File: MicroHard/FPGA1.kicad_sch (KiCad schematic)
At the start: 1 part, among them U4 XC7A100T-FTG256

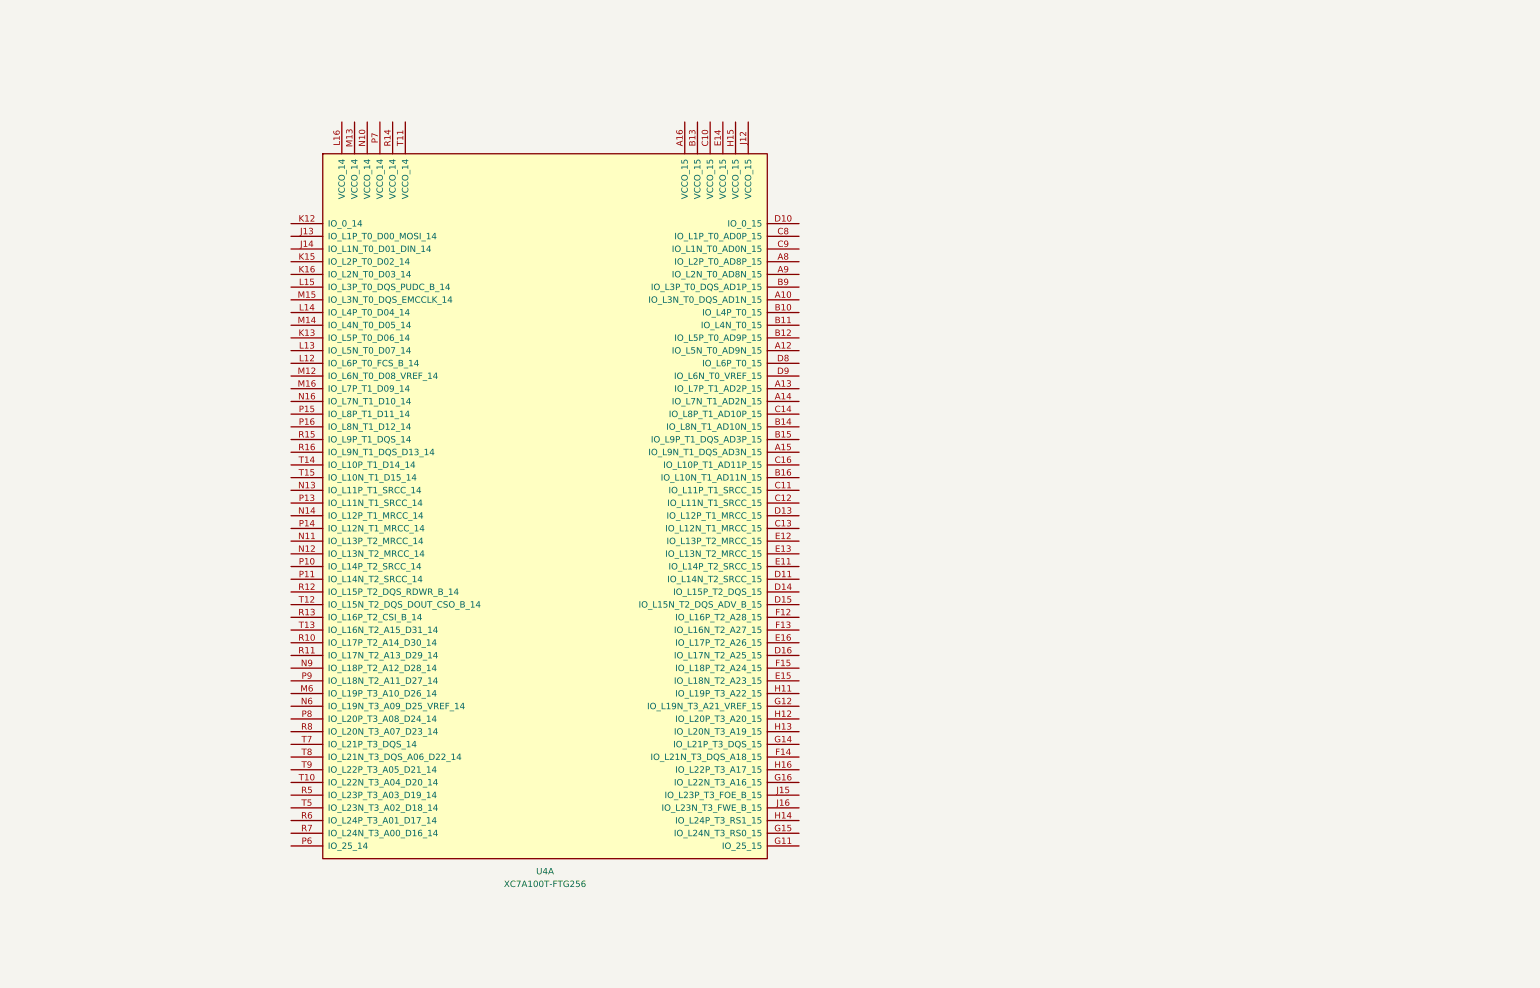
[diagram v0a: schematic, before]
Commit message: feat: finished FPGA config
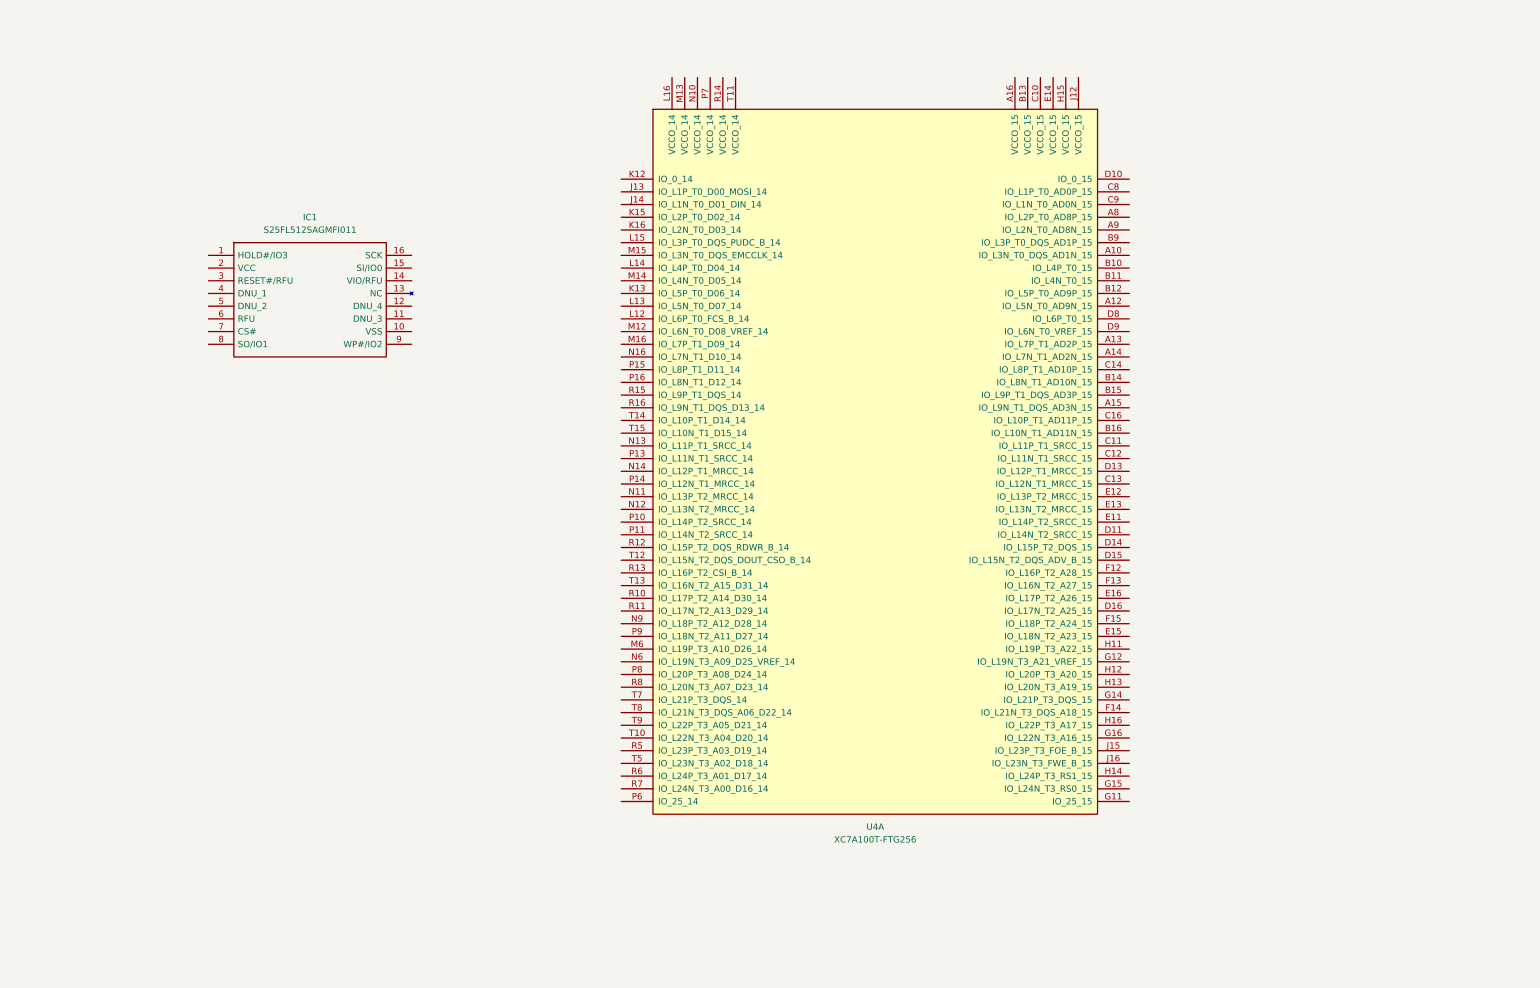
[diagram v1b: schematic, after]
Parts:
- added IC1: S25FL512SAGMFI011, SOIC127P1030X265-16N, symbol S25FL512SAGMFI011:S25FL512SAGMFI011
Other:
- moved on the sheet: U4A
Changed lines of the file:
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@@
 	(paper "A4")
 	(symbol
+		(lib_id "S25FL512SAGMFI011:S25FL512SAGMFI011")
+		(at 24.13 52.07 0)
+		(unit 1)
+		(exclude_from_sim no)
+		(in_bom yes)
+		(on_board yes)
+		(dnp no)
+		(fields_autoplaced yes)
+		(property "Reference" "IC1"
+			(at 44.45 44.45 0)
+			(effects
+				(font
+					(size 1.27 1.27)
+				)
+			)
+		)
+		(property "Value" "S25FL512SAGMFI011"
+			(at 44.45 46.99 0)
+			(effects
+				(font
+					(size 1.27 1.27)
+				)
+			)
+		)
+		(property "Footprint" "SOIC127P1030X265-16N"
+			(at 60.96 49.53 0)
+			(effects
+				(font
+					(size 1.27 1.27)
+				)
+				(justify left)
+				(hide yes)
+			)
+		)
+		(property "Datasheet" "http://www.cypress.com/file/177971/download"
+			(at 60.96 52.07 0)
+			(effects
+				(font
+					(size 1.27 1.27)
+				)
+				(justify left)
+				(hide yes)
+			)
+		)
+		(property "Description" "Flash,512Mbit,QSPI,133MHz,3V,SOIC16 S25FL512SAGMFI011, SPI NOR Flash Memory, 128M x 4 bit, 256M x 2 bit, 512M x 1 bit 512Mbit, 2.7  3.6 V, 16-Pin"
+			(at 24.13 52.07 0)
+			(effects
+				(font
+					(size 1.27 1.27)
+				)
+				(hide yes)
+			)
+		)
+		(property "Description_1" "Flash,512Mbit,QSPI,133MHz,3V,SOIC16 S25FL512SAGMFI011, SPI NOR Flash Memory, 128M x 4 bit, 256M x 2 bit, 512M x 1 bit 512Mbit, 2.7  3.6 V, 16-Pin"
+			(at 60.96 54.61 0)
+			(effects
+				(font
+					(size 1.27 1.27)
+				)
+				(justify left)
+				(hide yes)
+			)
+		)
+		(property "Height" "2.65"
+			(at 60.96 57.15 0)
+			(effects
+				(font
+					(size 1.27 1.27)
+				)
+				(justify left)
+				(hide yes)
+			)
+		)
+		(property "Mouser Part Number" "797-25FL512SAGMFI011"
+			(at 60.96 59.69 0)
+			(effects
+				(font
+					(size 1.27 1.27)
+				)
+				(justify left)
+				(hide yes)
+			)
+		)
+		(property "Mouser Price/Stock" "https://www.mouser.co.uk/ProductDetail/Cypress-Spansion/S25FL512SAGMFI011?qs=rDGpJoRV1kJ%252BPU3pl%252BHK1A%3D%3D"
+			(at 60.96 62.23 0)
+			(effects
+				(font
+					(size 1.27 1.27)
+				)
+				(justify left)
+				(hide yes)
+			)
+		)
+		(property "Manufacturer_Name" "Infineon"
+			(at 60.96 64.77 0)
+			(effects
+				(font
+					(size 1.27 1.27)
+				)
+				(justify left)
+				(hide yes)
+			)
+		)
+		(property "Manufacturer_Part_Number" "S25FL512SAGMFI011"
+			(at 60.96 67.31 0)
+			(effects
+				(font
+					(size 1.27 1.27)
+				)
+				(justify left)
+				(hide yes)
+			)
+		)
+		(pin "7"
+		)
+		(pin "6"
+		)
+		(pin "8"
+		)
+		(pin "1"
+		)
+		(pin "12"
+		)
+		(pin "10"
+		)
+		(pin "11"
+		)
+		(pin "4"
+		)
+		(pin "5"
+		)
+		(pin "13"
+		)
+		(pin "15"
+		)
+		(pin "3"
+		)
+		(pin "9"
+		)
+		(pin "2"
+		)
+		(pin "16"
+		)
+		(pin "14"
+		)
+		(instances
+			(project "MicroHard"
+				(path "/578bd531-a491-4b15-a479-460d159ffc14/e381883e-e672-4900-88a5-08b94f970a88/1131f32d-45e2-48d4-a5b0-b9e8f8db47f2"
+					(reference "IC1")
+					(unit 1)
+				)
+			)
+		)
+	)
+	(symbol
 		(lib_id "FPGA_Xilinx_Artix7:XC7A100T-FTG256")
-		(at 91.44 99.06 0)
+		(at 157.48 90.17 0)
 		(unit 1)
 		(exclude_from_sim no)
@@
 		(fields_autoplaced yes)
 		(property "Reference" "U4"
-			(at 91.44 175.26 0)
+			(at 157.48 166.37 0)
 			(effects
 				(font
@@
 		)
 		(property "Value" "XC7A100T-FTG256"
-			(at 91.44 177.8 0)
+			(at 157.48 168.91 0)
 			(effects
 				(font
@@
 		)
 		(property "Footprint" ""
-			(at 91.44 99.06 0)
+			(at 157.48 90.17 0)
 			(effects
 				(font
@@
 		)
 		(property "Datasheet" ""
-			(at 91.44 99.06 0)
+			(at 157.48 90.17 0)
 			(effects
 				(font
@@
 		)
 		(property "Description" "Artix 7 T 100 XC7A100T-FTG256"
-			(at 91.44 99.06 0)
-			(effects
-				(font
+			(at 157.48 90.17 0)
+			(effects
+				(font

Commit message: feat: finished Flash mem and FPGA Config
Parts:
- removed IC1: S25FL512SAGMFI011, SOIC127P1030X265-16N, symbol S25FL512SAGMFI011:S25FL512SAGMFI011
- added C45: 100u, symbol Device:C_Polarized_US
- added C46, C47: 4.7u, symbol Device:C
- added C48, C49, C50, C51: 470n, symbol Device:C
- added C52: 100n, symbol Device:C
- added R20, R22: 4.7k, symbol Device:R
- added R21: 2.4k, symbol Device:R
- added U5: MT25QL256ABA8ESF-0SIT, symbol MicroHardLibrary:MT25QL256ABA8ESF-0SIT
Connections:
- net DQ0: now reaches U4.J13 (IO_L1P_T0_D00_MOSI_14)
- net DQ0: now also U5.15 (DQ0)
- net DQ1: now reaches U4.J14 (IO_L1N_T0_D01_DIN_14)
- net DQ1: now also U5.8 (DQ1)
- net W#: now reaches U4.K15 (IO_L2P_T0_D02_14)
- net W#: now also R22.2, U5.9 (W#/DQ2)
- net HOLD#: now reaches U4.K16 (IO_L2N_T0_D03_14)
- net HOLD#: now also R20.2, U5.1 (DQ3/HOLD#)
- net CS#: now reaches U4.L12 (IO_L6P_T0_FCS_B_14)
- net CS#: now also R21.2, U5.7 (S#)
- net GND: now reaches U4.L15 (IO_L3P_T0_DQS_PUDC_B_14)
- net GND: now also C45.2, C46.2, C47.2, C48.2, C49.2, C50.2, C51.2, C52.2, U5.10 (Vss)
- net +3.3V: now reaches U4.L16 (VCCO_14)
- net +3.3V: now also U4.M13 (VCCO_14), U4.N10 (VCCO_14), U4.P7 (VCCO_14), U4.R14 (VCCO_14), U4.T11 (VCCO_14), C45.1, C46.1, C47.1, C48.1, C49.1, C50.1, C51.1, C52.1, R20.1, R21.1, R22.1, U5.2 (Vcc)
- new net FPGA_CONFIG_CLOCK: U5.16 (C)
- no-connect marks 0 -> 2
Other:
- moved on the sheet: U4A

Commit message: feat: finished config
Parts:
- added C53: 10n, symbol Device:C
- added C54: 30p, symbol Device:C
- added Y1: CB3-3C-20M000000, CB3-3C-20M000000:OSC_CB3-3C-20M000000, symbol CB3-3C-20M000000:CB3-3C-20M000000
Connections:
- net +3.3V: now also C53.1, Y1.1 (EOH), Y1.4 (VCC)
- net GND: now also C53.2, C54.2, Y1.2 (GND)
- net at U4.N11 (IO_L13P_T2_MRCC_14): now also C54.1, Y1.3 (OUTPUT)
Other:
- note added: "Oscillator with stability +- 50 ppm"

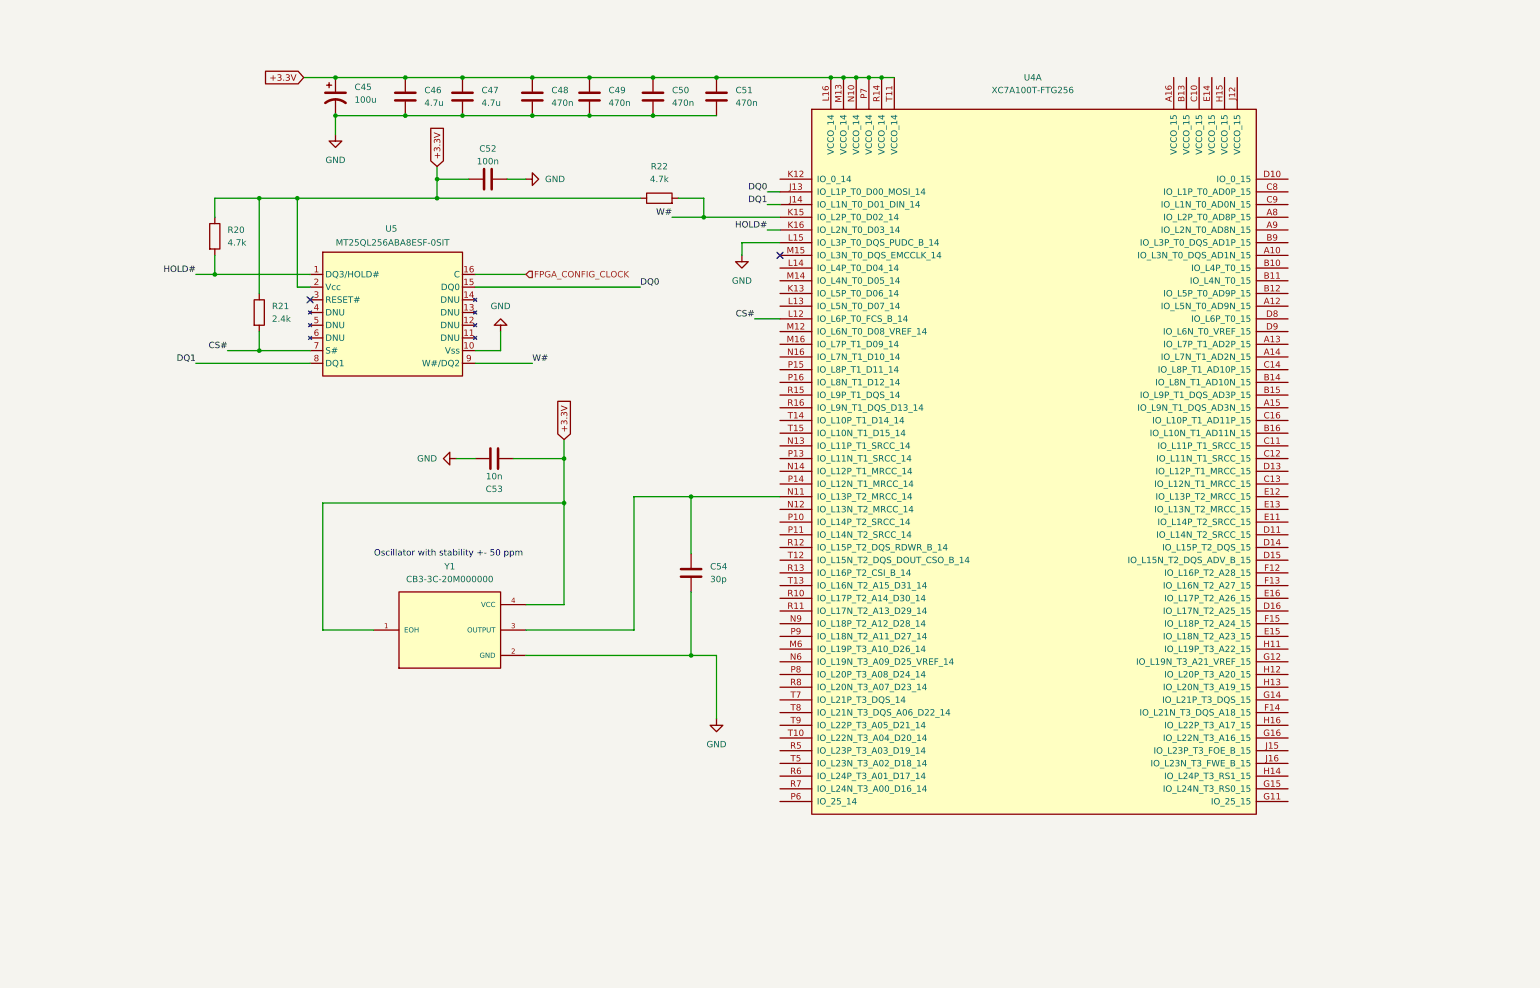
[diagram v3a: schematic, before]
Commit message: feat: added VGA signal out from FPGA
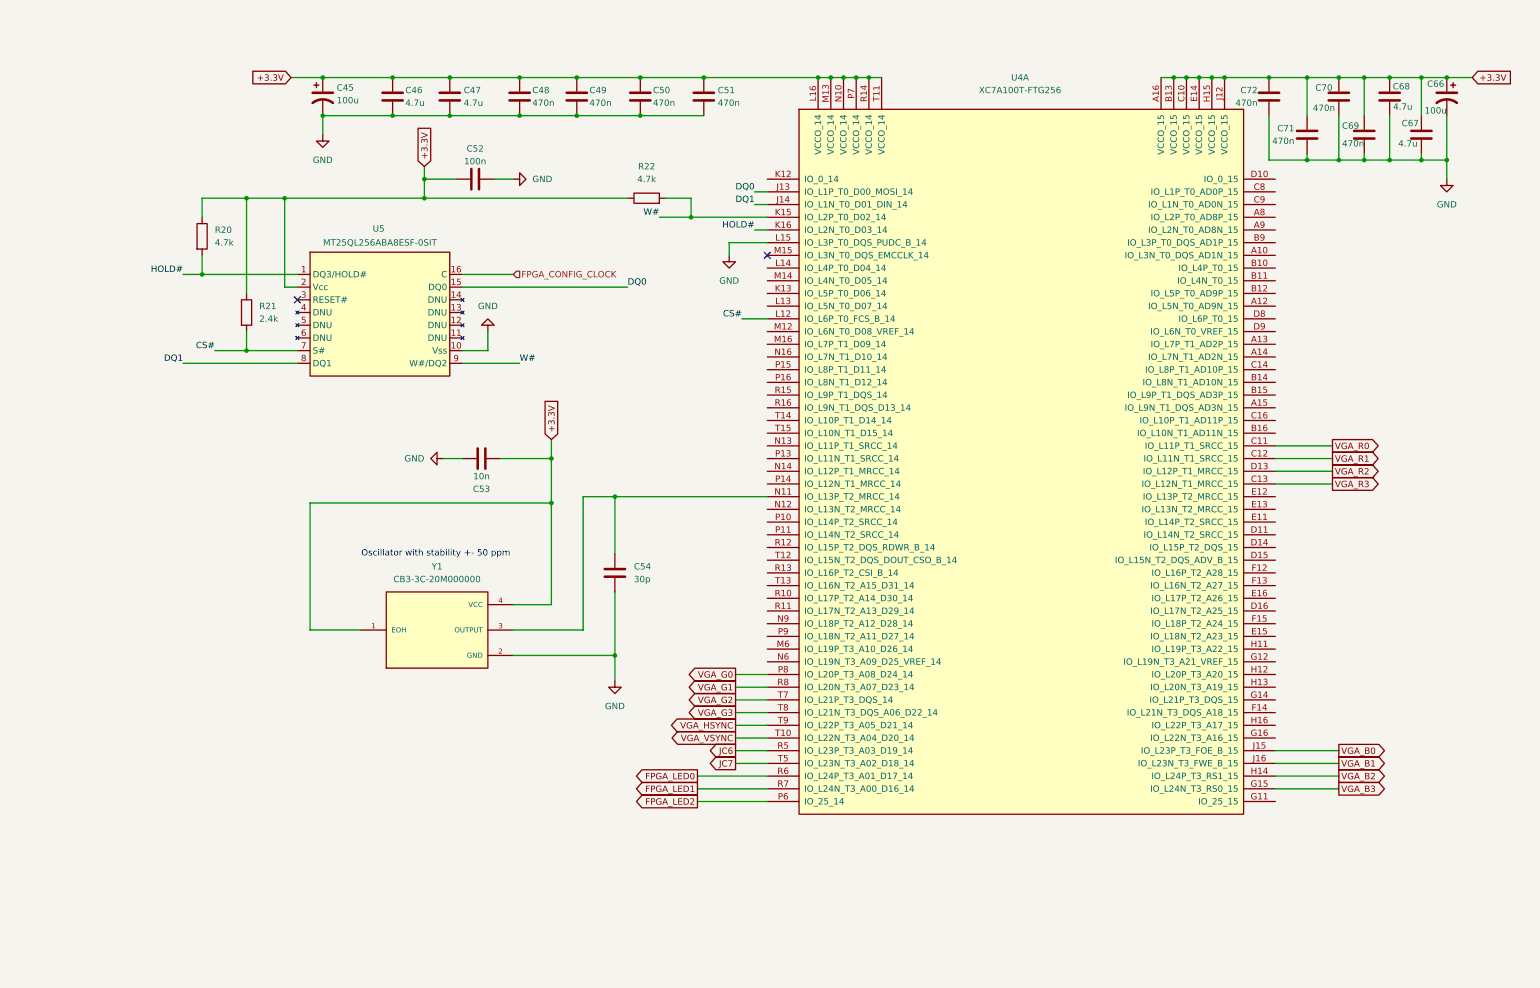
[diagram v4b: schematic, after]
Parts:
- added C66: 100u, symbol Device:C_Polarized_US
- added C67, C68: 4.7u, symbol Device:C
- added C69, C70, C71, C72: 470n, symbol Device:C
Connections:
- net +3.3V: now also U4.A16 (VCCO_15), U4.B13 (VCCO_15), U4.C10 (VCCO_15), U4.E14 (VCCO_15), U4.H15 (VCCO_15), U4.J12 (VCCO_15), C66.1, C67.1, C68.1, C69.1, C70.1, C71.1, C72.1
- net GND: now also C66.2, C67.2, C68.2, C69.2, C70.2, C71.2, C72.2
- net VGA_R0: now reaches U4.C11 (IO_L11P_T1_SRCC_15)
- net VGA_R1: now reaches U4.C12 (IO_L11N_T1_SRCC_15)
- net VGA_R3: now reaches U4.C13 (IO_L12N_T1_MRCC_15)
- net VGA_R2: now reaches U4.D13 (IO_L12P_T1_MRCC_15)
- net VGA_B3: now reaches U4.G15 (IO_L24N_T3_RS0_15)
- net VGA_B2: now reaches U4.H14 (IO_L24P_T3_RS1_15)
- net VGA_B0: now reaches U4.J15 (IO_L23P_T3_FOE_B_15)
- net VGA_B1: now reaches U4.J16 (IO_L23N_T3_FWE_B_15)
- net FPGA_LED2: now reaches U4.P6 (IO_25_14)
- net VGA_G0: now reaches U4.P8 (IO_L20P_T3_A08_D24_14)
- net JC6: now reaches U4.R5 (IO_L23P_T3_A03_D19_14)
- net FPGA_LED0: now reaches U4.R6 (IO_L24P_T3_A01_D17_14)
- net FPGA_LED1: now reaches U4.R7 (IO_L24N_T3_A00_D16_14)
- net VGA_G1: now reaches U4.R8 (IO_L20N_T3_A07_D23_14)
- net VGA_VSYNC: now reaches U4.T10 (IO_L22N_T3_A04_D20_14)
- net JC7: now reaches U4.T5 (IO_L23N_T3_A02_D18_14)
- net VGA_G2: now reaches U4.T7 (IO_L21P_T3_DQS_14)
- net VGA_G3: now reaches U4.T8 (IO_L21N_T3_DQS_A06_D22_14)
- net VGA_HSYNC: now reaches U4.T9 (IO_L22P_T3_A05_D21_14)
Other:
- moved on the sheet: C45, C46, C47, C48, C49, C50, C51, C52, C53, C54, R20, R21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
